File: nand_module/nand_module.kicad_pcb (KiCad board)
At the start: 2 copper layers, 47.1 x 30.9 mm, 19 parts, among them J1 BUS_A, J2 BUS_B

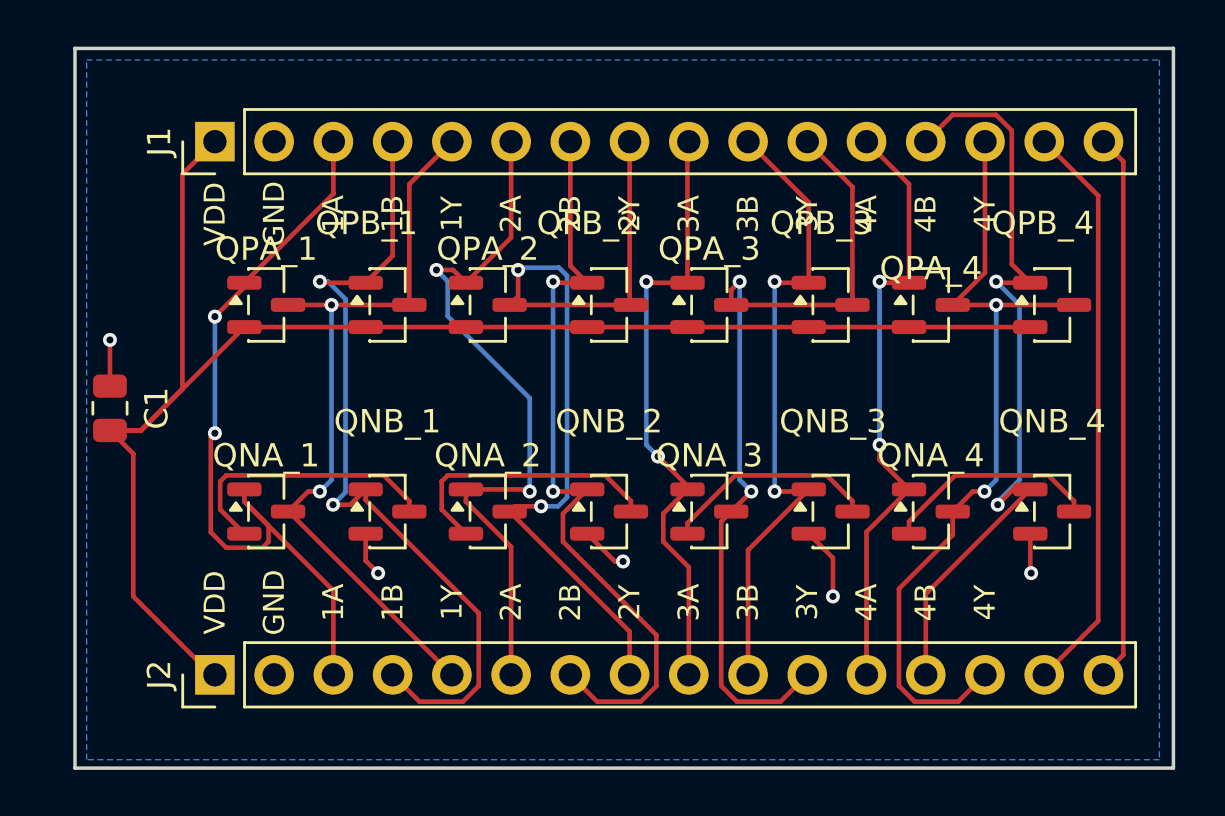
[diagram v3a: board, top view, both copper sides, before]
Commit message: Tidy NAND board labels: QPA1 form + ref text off the pin labels
Ran tidy_labels.py (in history) over the routed board: 16 refs
QPA_1->QPA1 etc., their reference text moved into the central gap at
0.8 mm. 240 track objects and all net names unchanged.
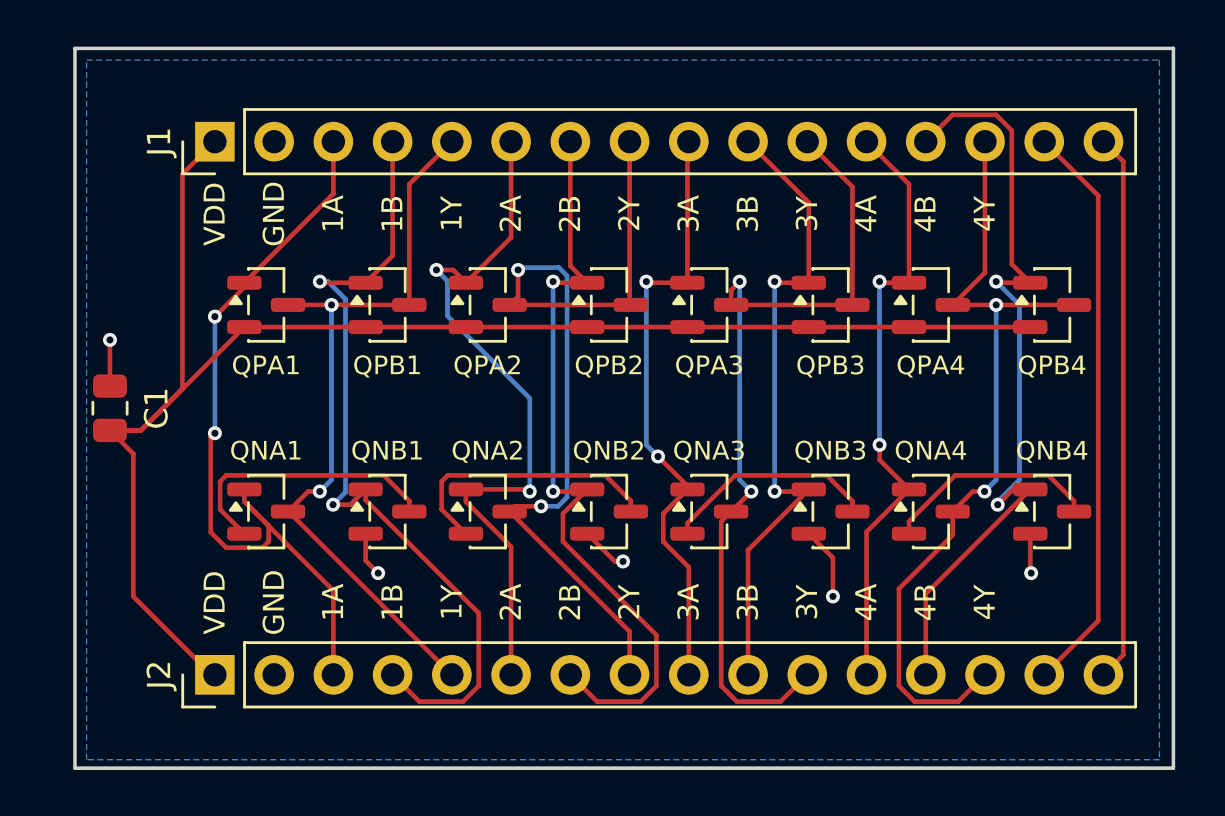
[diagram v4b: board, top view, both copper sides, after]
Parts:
- renumbered QNA_1 to QNA1, QNA_2 to QNA2, QNA_3 to QNA3, QNA_4 to QNA4, QNB_1 to QNB1, QNB_2 to QNB2, QNB_3 to QNB3, QNB_4 to QNB4, QPA_1 to QPA1, QPA_2 to QPA2, QPA_3 to QPA3, QPA_4 to QPA4, QPB_1 to QPB1, QPB_2 to QPB2, QPB_3 to QPB3, QPB_4 to QPB4
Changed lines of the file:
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@@
 		(descr "SOT, 3 Pin (JEDEC TO-236 Var AB https://www.jedec.org/document_search?search_api_views_fulltext=TO-236)")
 		(tags "SOT TO_SOT_SMD")
-		(property "Reference" "QPA_2"
-			(at 0 -2.4 0)
+		(property "Reference" "QPA2"
+			(at 0 2.6 0)
 			(layer "F.SilkS")
 			(effects
 				(font
-					(size 1 1)
-					(thickness 0.15)
+					(size 0.8 0.8)
+					(thickness 0.12)
 				)
 			)
@@
 		(descr "SOT, 3 Pin (JEDEC TO-236 Var AB https://www.jedec.org/document_search?search_api_views_fulltext=TO-236)")
 		(tags "SOT TO_SOT_SMD")
-		(property "Reference" "QNA_4"
-			(at 0 -2.4 0)
+		(property "Reference" "QNA4"
+			(at 0 -2.6 0)
 			(layer "F.SilkS")
 			(effects
 				(font
-					(size 1 1)
-					(thickness 0.15)
+					(size 0.8 0.8)
+					(thickness 0.12)
 				)
 			)
@@
 		(descr "SOT, 3 Pin (JEDEC TO-236 Var AB https://www.jedec.org/document_search?search_api_views_fulltext=TO-236)")
 		(tags "SOT TO_SOT_SMD")
-		(property "Reference" "QNB_3"
-			(at 0.1 -3.86 0)
+		(property "Reference" "QNB3"
+			(at 0 -2.6 0)
 			(layer "F.SilkS")
 			(effects
 				(font
-					(size 1 1)
-					(thickness 0.15)
+					(size 0.8 0.8)
+					(thickness 0.12)
 				)
 			)
@@
 		(descr "SOT, 3 Pin (JEDEC TO-236 Var AB https://www.jedec.org/document_search?search_api_views_fulltext=TO-236)")
 		(tags "SOT TO_SOT_SMD")
-		(property "Reference" "QNB_2"
-			(at 0 -3.86 0)
+		(property "Reference" "QNB2"
+			(at 0 -2.6 0)
 			(layer "F.SilkS")
 			(effects
 				(font
-					(size 1 1)
-					(thickness 0.15)
+					(size 0.8 0.8)
+					(thickness 0.12)
 				)
 			)
@@
 		(descr "SOT, 3 Pin (JEDEC TO-236 Var AB https://www.jedec.org/document_search?search_api_views_fulltext=TO-236)")
 		(tags "SOT TO_SOT_SMD")
-		(property "Reference" "QPB_3"
-			(at -0.4 -3.5 0)
+		(property "Reference" "QPB3"
+			(at 0 2.6 0)
 			(layer "F.SilkS")
 			(effects
 				(font
-					(size 1 1)
-					(thickness 0.15)
+					(size 0.8 0.8)
+					(thickness 0.12)
 				)
 			)
@@
 		(descr "SOT, 3 Pin (JEDEC TO-236 Var AB https://www.jedec.org/document_search?search_api_views_fulltext=TO-236)")
 		(tags "SOT TO_SOT_SMD")
-		(property "Reference" "QNB_1"
-			(at 0 -3.86 0)
+		(property "Reference" "QNB1"
+			(at 0 -2.6 0)
 			(layer "F.SilkS")
 			(effects
 				(font
-					(size 1 1)
-					(thickness 0.15)
+					(size 0.8 0.8)
+					(thickness 0.12)
 				)
 			)
@@
 		(descr "SOT, 3 Pin (JEDEC TO-236 Var AB https://www.jedec.org/document_search?search_api_views_fulltext=TO-236)")
 		(tags "SOT TO_SOT_SMD")
-		(property "Reference" "QNA_1"
-			(at 0 -2.4 0)
+		(property "Reference" "QNA1"
+			(at 0 -2.6 0)
 			(layer "F.SilkS")
 			(effects
 				(font
-					(size 1 1)
-					(thickness 0.15)
+					(size 0.8 0.8)
+					(thickness 0.12)
 				)
 			)
@@
 		(descr "SOT, 3 Pin (JEDEC TO-236 Var AB https://www.jedec.org/document_search?search_api_views_fulltext=TO-236)")
 		(tags "SOT TO_SOT_SMD")
-		(property "Reference" "QNA_3"
-			(at 0 -2.4 0)
+		(property "Reference" "QNA3"
+			(at 0 -2.6 0)
 			(layer "F.SilkS")
 			(effects
 				(font
-					(size 1 1)
-					(thickness 0.15)
+					(size 0.8 0.8)
+					(thickness 0.12)
 				)
 			)
@@
 		(descr "SOT, 3 Pin (JEDEC TO-236 Var AB https://www.jedec.org/document_search?search_api_views_fulltext=TO-236)")
 		(tags "SOT TO_SOT_SMD")
-		(property "Reference" "QPA_1"
-			(at 0 -2.4 0)
+		(property "Reference" "QPA1"
+			(at 0 2.6 0)
 			(layer "F.SilkS")
 			(effects
 				(font
-					(size 1 1)
-					(thickness 0.15)
+					(size 0.8 0.8)
+					(thickness 0.12)
 				)
 			)
@@
 		(descr "SOT, 3 Pin (JEDEC TO-236 Var AB https://www.jedec.org/document_search?search_api_views_fulltext=TO-236)")
 		(tags "SOT TO_SOT_SMD")
-		(property "Reference" "QNA_2"
-			(at 0 -2.4 0)
+		(property "Reference" "QNA2"
+			(at 0 -2.6 0)
 			(layer "F.SilkS")
 			(effects
 				(font
-					(size 1 1)
-					(thickness 0.15)
+					(size 0.8 0.8)
+					(thickness 0.12)
 				)
 			)
@@
 		(descr "SOT, 3 Pin (JEDEC TO-236 Var AB https://www.jedec.org/document_search?search_api_views_fulltext=TO-236)")
 		(tags "SOT TO_SOT_SMD")
-		(property "Reference" "QPA_3"
-			(at 0 -2.4 0)
+		(property "Reference" "QPA3"
+			(at 0 2.6 0)
 			(layer "F.SilkS")
 			(effects
 				(font
-					(size 1 1)
-					(thickness 0.15)
+					(size 0.8 0.8)
+					(thickness 0.12)
 				)
 			)
@@
 		(descr "SOT, 3 Pin (JEDEC TO-236 Var AB https://www.jedec.org/document_search?search_api_views_fulltext=TO-236)")
 		(tags "SOT TO_SOT_SMD")
-		(property "Reference" "QNB_4"
-			(at 0 -3.86 0)
+		(property "Reference" "QNB4"
+			(at 0 -2.6 0)
 			(layer "F.SilkS")
 			(effects
 				(font
-					(size 1 1)
-					(thickness 0.15)
+					(size 0.8 0.8)
+					(thickness 0.12)
 				)
 			)
@@
 		(descr "SOT, 3 Pin (JEDEC TO-236 Var AB https://www.jedec.org/document_search?search_api_views_fulltext=TO-236)")
 		(tags "SOT TO_SOT_SMD")
-		(property "Reference" "QPA_4"
-			(at 0 -1.56 0)
+		(property "Reference" "QPA4"
+			(at 0 2.6 0)
 			(layer "F.SilkS")
 			(effects
 				(font
-					(size 1 1)
-					(thickness 0.15)
+					(size 0.8 0.8)
+					(thickness 0.12)
 				)
 			)
@@
 		(descr "SOT, 3 Pin (JEDEC TO-236 Var AB https://www.jedec.org/document_search?search_api_views_fulltext=TO-236)")
 		(tags "SOT TO_SOT_SMD")
-		(property "Reference" "QPB_1"
-			(at -0.9 -3.5 0)
+		(property "Reference" "QPB1"
+			(at 0 2.6 0)
 			(layer "F.SilkS")
 			(effects
 				(font
-					(size 1 1)
-					(thickness 0.15)
+					(size 0.8 0.8)
+					(thickness 0.12)
 				)
 			)
@@
 		(descr "SOT, 3 Pin (JEDEC TO-236 Var AB https://www.jedec.org/document_search?search_api_views_fulltext=TO-236)")
 		(tags "SOT TO_SOT_SMD")
-		(property "Reference" "QPB_4"
-			(at -0.4 -3.5 0)
+		(property "Reference" "QPB4"
+			(at 0 2.6 0)
 			(layer "F.SilkS")
 			(effects
 				(font
-					(size 1 1)
-					(thickness 0.15)
+					(size 0.8 0.8)
+					(thickness 0.12)
 				)
 			)
@@
 		(descr "SOT, 3 Pin (JEDEC TO-236 Var AB https://www.jedec.org/document_search?search_api_views_fulltext=TO-236)")
 		(tags "SOT TO_SOT_SMD")
-		(property "Reference" "QPB_2"
-			(at -0.9 -3.5 0)
+		(property "Reference" "QPB2"
+			(at 0 2.6 0)
 			(layer "F.SilkS")
 			(effects
 				(font
-					(size 1 1)
-					(thickness 0.15)
+					(size 0.8 0.8)
+					(thickness 0.12)
 				)
 			)

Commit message: Label the two spare bus pins (BX/BY) on both headers
Reran label_headers.py over the board: silk labels 28 -> 32 (BX/BY added
at pins 15/16). 240 track objects, refs and net names unchanged.
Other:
- board text added: "BX"
- board text added: "BY"
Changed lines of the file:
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@@
+		)
+	)
+	(gr_text "BX"
+		(at 55.56 23.1 90)
+		(layer "F.SilkS")
+		(effects
+			(font
+				(size 0.9 0.9)
+				(thickness 0.14)
+			)
+		)
+	)
+	(gr_text "BX"
+		(at 55.56 39.76 90)
+		(layer "F.SilkS")
+		(effects
+			(font
+				(size 0.9 0.9)
+				(thickness 0.14)
+			)
+		)
+	)
+	(gr_text "BY"
+		(at 58.1 23.1 90)
+		(layer "F.SilkS")
+		(effects
+			(font
+				(size 0.9 0.9)
+				(thickness 0.14)
+			)
+		)
+	)
+	(gr_text "BY"
+		(at 58.1 39.76 90)
+		(layer "F.SilkS")
+		(effects
+			(font
+				(size 0.9 0.9)
+				(thickness 0.14)
+			)
 		)
 	)

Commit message: Relabel nand/indicator board FETs BSS -> AO34xxA (value text only)
AO3400A/AO3401A are pin-compatible SOT-23 drop-ins for BSS138/BSS84, so only
the silkscreen Value changes. Routing (nand: 211 segments, 29 vias, GND zone),
placement and labels untouched. Boards verified to load in pcbnew.
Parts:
- QNA1, QNA2, QNA3, QNA4, QNB1, QNB2, QNB3, QNB4: value BSS138 -> AO3400A
- QPA1, QPA2, QPA3, QPA4, QPB1, QPB2, QPB3, QPB4: value BSS84 -> AO3401A
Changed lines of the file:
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@@
 			)
 		)
-		(property "Value" "BSS84"
+		(property "Value" "AO3401A"
 			(at 0 2.4 0)
 			(layer "F.Fab")
@@
 			)
 		)
-		(property "Value" "BSS138"
+		(property "Value" "AO3400A"
 			(at 0 2.4 0)
 			(layer "F.Fab")
@@
 			)
 		)
-		(property "Value" "BSS138"
+		(property "Value" "AO3400A"
 			(at 0 2.4 0)
 			(layer "F.Fab")
@@
 			)
 		)
-		(property "Value" "BSS138"
+		(property "Value" "AO3400A"
 			(at 0 2.4 0)
 			(layer "F.Fab")
@@
 			)
 		)
-		(property "Value" "BSS84"
+		(property "Value" "AO3401A"
 			(at 0 2.4 0)
 			(layer "F.Fab")
@@
 			)
 		)
-		(property "Value" "BSS138"
+		(property "Value" "AO3400A"
 			(at 0 2.4 0)
 			(layer "F.Fab")
@@
 			)
 		)
-		(property "Value" "BSS138"
+		(property "Value" "AO3400A"
 			(at 0 2.4 0)
 			(layer "F.Fab")
@@
 			)
 		)
-		(property "Value" "BSS138"
+		(property "Value" "AO3400A"
 			(at 0 2.4 0)
 			(layer "F.Fab")
@@
 			)
 		)
-		(property "Value" "BSS84"
+		(property "Value" "AO3401A"
 			(at 0 2.4 0)
 			(layer "F.Fab")
@@
 			)
 		)
-		(property "Value" "BSS138"
+		(property "Value" "AO3400A"
 			(at 0 2.4 0)
 			(layer "F.Fab")
@@
 			)
 		)
-		(property "Value" "BSS84"
+		(property "Value" "AO3401A"
 			(at 0 2.4 0)
 			(layer "F.Fab")
@@
 			)
 		)
-		(property "Value" "BSS138"
+		(property "Value" "AO3400A"
 			(at 0 2.4 0)
 			(layer "F.Fab")
@@
 			)
 		)
-		(property "Value" "BSS84"
+		(property "Value" "AO3401A"
 			(at 0 2.4 0)
 			(layer "F.Fab")
@@
 			)
 		)
-		(property "Value" "BSS84"
+		(property "Value" "AO3401A"
 			(at 0 2.4 0)
 			(layer "F.Fab")
@@
 			)
 		)
-		(property "Value" "BSS84"
+		(property "Value" "AO3401A"
 			(at 0 2.4 0)
 			(layer "F.Fab")
@@
 			)
 		)
-		(property "Value" "BSS84"
+		(property "Value" "AO3401A"
 			(at 0 2.4 0)
 			(layer "F.Fab")

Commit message: Sync nand board header value to BUS_STACK_1x16
Last remaining divergence from the netlist (J1/J2 were BUS_A/BUS_B).
Refs, nets and FET values already matched. Routing untouched: 211
segments, 29 vias, GND zone; verified in pcbnew.
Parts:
- J1: value BUS_A -> BUS_STACK_1x16
- J2: value BUS_B -> BUS_STACK_1x16
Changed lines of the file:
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@@
 			)
 		)
-		(property "Value" "BUS_B"
+		(property "Value" "BUS_STACK_1x16"
 			(at 0 40.48 90)
 			(layer "F.Fab")
@@
 			)
 		)
-		(property "Value" "BUS_A"
+		(property "Value" "BUS_STACK_1x16"
 			(at 0 40.48 90)
 			(layer "F.Fab")
